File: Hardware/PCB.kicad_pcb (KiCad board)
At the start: 2 copper layers, 41 parts, among them Q5 NMOS, Q6 NMOS, Q7 NMOS, Q8 NMOS, U10 TLV379IDR, U11 LM780_TO220_MA BYC_3V_BO_POJD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, U6 ESP32-WROOM-32, U7 STM32L432KCUx, U8 IR2102, U9 IR2102

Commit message: New update
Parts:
- removed C15: C_Polarized, Capacitor_SMD:CP_Elec_5x5.3
- removed U7: STM32L432KCUx, Package_DFN_QFN:QFN-32-1EP_5x5mm_P0.5mm_EP3.45x3.45mm
- added C23: 1uF, Capacitor_SMD:C_1206_3216Metric, F.Cu at (204.2, 88.6)
- added J1: Conn_01x15, Connector_Molex:Molex_SL_171971-0015_1x15_P2.54mm_Vertical, F.Cu at (229.4, 122.9)
- added J2: Conn_01x15, Connector_Molex:Molex_SL_171971-0015_1x15_P2.54mm_Vertical, F.Cu at (238.1, 122.9)
- C13: value C -> 1uF
- D4, D6: footprint Diode_SMD:D_SOD-523 -> Diode_SMD:D_MiniMELF
- moved H3 106.7 mm to (267.4, 103.3)
- moved H4 106.7 mm to (267.4, 110.5)
- moved D4 80.1 mm to (186.8, 65.4)
- moved D6 71.1 mm to (178.3, 71.8)
- moved Q8 66.8 mm to (76.3, 90.2)
- moved Q5 66.5 mm to (41.7, 89.8)
- moved Q6 66.5 mm to (53.2, 89.8)
- moved Q7 66.5 mm to (64.8, 89.8)
- moved R9 61.3 mm to (190.6, 104.4)
- moved R11 59.7 mm to (190.0, 111.2)
- moved R13 56.2 mm to (198.1, 96.3)
- moved H1 56.1 mm to (185.9, 128.3), turned to 180 degrees
- moved R16 56.1 mm to (198.0, 108.9)
- moved R18 55.7 mm to (198.1, 104.4)
- moved R10 54.0 mm to (190.8, 99.1)
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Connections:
- C12 pad 1: /TX -> Net-(J1-Pin_4)
- D6 pad 1: Net-(D6-A) -> Net-(D6-K)
- R9 pad 1: /TX -> Net-(J1-Pin_4)
- U6 pad 1: GND -> unconnected-(U6-GND-Pad1)_23
- U6 pad 15: GND -> unconnected-(U6-GND-Pad1)_12
- U6 pad 2: Net-(U10-V+) -> unconnected-(U6-VDD-Pad2)
- U6 pad 33: unconnected-(U6-IO21-Pad33) -> /SCK
- U6 pad 36: unconnected-(U6-IO22-Pad36) -> /MISO
- U6 pad 37: unconnected-(U6-IO23-Pad37) -> /MOSI
- U6 pad 38: GND -> unconnected-(U6-GND-Pad1)_2
- U6 pad 39: GND -> unconnected-(U6-GND-Pad1)_11
- U9 pad 8: Net-(D6-A) -> Net-(D6-K)

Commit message: 1
1
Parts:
- moved H4 240.1 mm to (34.0, 54.0)
- moved H3 236.7 mm to (33.0, 70.5)
- moved H1 155.0 mm to (34.2, 96.7)
- moved H2 152.4 mm to (34.2, 106.2)
- moved U11 88.4 mm to (92.2, 127.2), turned to 0 degrees
- moved C17 75.8 mm to (109.5, 109.0)
- moved C21 71.9 mm to (112.0, 113.5), turned to 90 degrees
- moved C18 69.4 mm to (114.5, 107.5), turned to -90 degrees
- moved R15 65.4 mm to (130.5, 65.5)
- moved C1 65.3 mm to (135.5, 58.5)
- moved C16 62.0 mm to (123.0, 83.5), turned to 90 degrees
- moved R11 62.0 mm to (133.0, 87.0), turned to 180 degrees
- moved R9 61.5 mm to (141.0, 68.0), turned to -90 degrees
- moved R10 53.8 mm to (140.0, 81.5)
- moved R18 53.7 mm to (144.5, 102.1)
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
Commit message: 1
1
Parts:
- removed U6: ESP32-WROOM-32, RF_Module:ESP32-WROOM-32
- added J3: Conn_01x19, Connector_PinHeader_2.54mm:PinHeader_1x19_P2.54mm_Vertical, F.Cu at (74.2, 69.9)
- added J4: Conn_01x19, Connector_PinHeader_2.54mm:PinHeader_1x19_P2.54mm_Vertical, F.Cu at (49.2, 69.9)
- J1, J2: footprint Connector_Molex:Molex_SL_171971-0015_1x15_P2.54mm_Vertical -> Connector_PinHeader_2.54mm:PinHeader_1x15_P2.54mm_Vertical
- moved J2 163.0 mm to (115.2, 27.0), turned to 0 degrees
- moved J1 152.4 mm to (100.0, 27.0), turned to 0 degrees
- moved H4 123.1 mm to (38.0, 177.0)
- moved R14 93.2 mm to (92.5, 112.5), turned to 90 degrees
- moved C1 78.6 mm to (151.5, 135.5), turned to 90 degrees
- moved R12 77.9 mm to (141.5, 118.5), turned to -90 degrees
- moved H3 73.8 mm to (40.0, 144.0)
- moved D6 70.0 mm to (134.8, 118.5), turned to 0 degrees
- moved C12 67.0 mm to (146.5, 135.5), turned to 90 degrees
- moved R9 67.0 mm to (141.5, 135.0), turned to 90 degrees
- moved C23 63.1 mm to (127.5, 113.5), turned to 90 degrees
- moved C13 57.8 mm to (127.0, 124.5), turned to 90 degrees
- moved R15 56.6 mm to (154.0, 117.0)
- moved C19 54.7 mm to (84.3, 128.0)
- moved R19 53.5 mm to (156.5, 135.5), turned to 90 degrees
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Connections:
- J1 pad 7: unconnected-(J1-Pin_7-Pad7) -> /CC
- J2 pad 1: /RX -> /TX
- J2 pad 2: /TX -> /RX

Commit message: 1
Płytka gotowa do trasowania ścieżek
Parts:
- moved R16 59.4 mm to (98.5, 115.0)
- moved R19 52.7 mm to (140.0, 85.5), turned to -90 degrees
- moved C1 52.6 mm to (135.0, 85.5), turned to -90 degrees
- moved U10 50.3 mm to (127.0, 77.0)
- moved R17 49.9 mm to (119.0, 76.5), turned to -90 degrees
- moved R11 49.7 mm to (124.5, 85.0), turned to 180 degrees
- moved H4 47.0 mm to (40.0, 130.0)
- moved R9 44.3 mm to (127.5, 93.0), turned to 180 degrees
- moved C12 43.8 mm to (138.0, 92.5)
- moved R15 43.6 mm to (138.0, 76.5), turned to -90 degrees
- moved H2 38.7 mm to (40.0, 80.0)
- moved H3 34.0 mm to (40.0, 110.0)
- moved H1 31.7 mm to (40.0, 60.0)
- moved J3 23.2 mm to (96.0, 77.9)
- moved J4 23.2 mm to (71.0, 77.9)
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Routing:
- net Net-(Q5-D): track 0.00 -> 37.4 mm

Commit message: 1
sortowanie kluczy ok
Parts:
- moved U9 55.9 mm to (81.8, 115.1)
- moved R12 50.2 mm to (87.4, 122.1), turned to -90 degrees
- moved C23 47.4 mm to (83.3, 122.1), turned to 90 degrees
- moved C22 46.4 mm to (161.0, 136.6)
- moved D5 46.4 mm to (163.0, 90.6)
- moved L2 46.4 mm to (160.2, 101.6)
- moved R11 46.4 mm to (170.4, 91.6)
- moved U11 46.4 mm to (158.7, 127.9)
- moved C14 46.2 mm to (160.7, 113.8)
- moved C16 46.2 mm to (163.2, 122.8)
- moved C21 46.2 mm to (156.1, 122.8)
- moved R13 45.4 mm to (84.0, 109.5)
- moved D6 44.5 mm to (85.3, 126.5)
- moved U8 36.5 mm to (102.8, 115.0)
- moved R10 34.0 mm to (108.1, 121.8), turned to -90 degrees
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
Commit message: 1
ogarnieta plytka, elementy rozmieszczone, zostalo zrobic sciezki
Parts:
- moved D5 52.2 mm to (118.0, 117.1), turned to 90 degrees
- moved R11 50.3 mm to (121.0, 82.5), turned to 90 degrees
- moved L2 49.0 mm to (111.2, 102.0)
- moved C22 45.3 mm to (116.0, 131.0), turned to -90 degrees
- moved C14 37.0 mm to (126.0, 101.0)
- moved R15 33.1 mm to (115.0, 89.5)
- moved U11 32.7 mm to (127.0, 120.0)
- moved C16 32.6 mm to (132.5, 112.0)
- moved C21 32.5 mm to (125.5, 112.0), turned to 0 degrees
- moved U10 30.6 mm to (107.0, 85.9), turned to 90 degrees
- moved C12 28.8 mm to (133.0, 82.5), turned to -90 degrees
- moved R9 27.2 mm to (127.0, 82.5), turned to 90 degrees
- moved C1 26.3 mm to (121.0, 89.5), turned to 90 degrees
- moved R19 25.4 mm to (127.0, 89.5), turned to 90 degrees
- moved R17 16.4 mm to (115.0, 82.5), turned to 90 degrees
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
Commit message: 05.05.25
Mamy bledy, chujowo jest
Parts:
- moved R10 1.00 mm to (107.0, 121.8)
- moved R12 0.41 mm to (87.0, 122.1)
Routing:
- net Net-(D6-K): track 0.00 -> 14.6 mm
- net Net-(U9-HO): track 0.00 -> 12.2 mm
- net Net-(U10-V+): track 0.00 -> 5.06 mm
- net Net-(D6-A): track 0.00 -> 3.42 mm
- net Net-(Q5-D): track 37.4 -> 34.3 mm

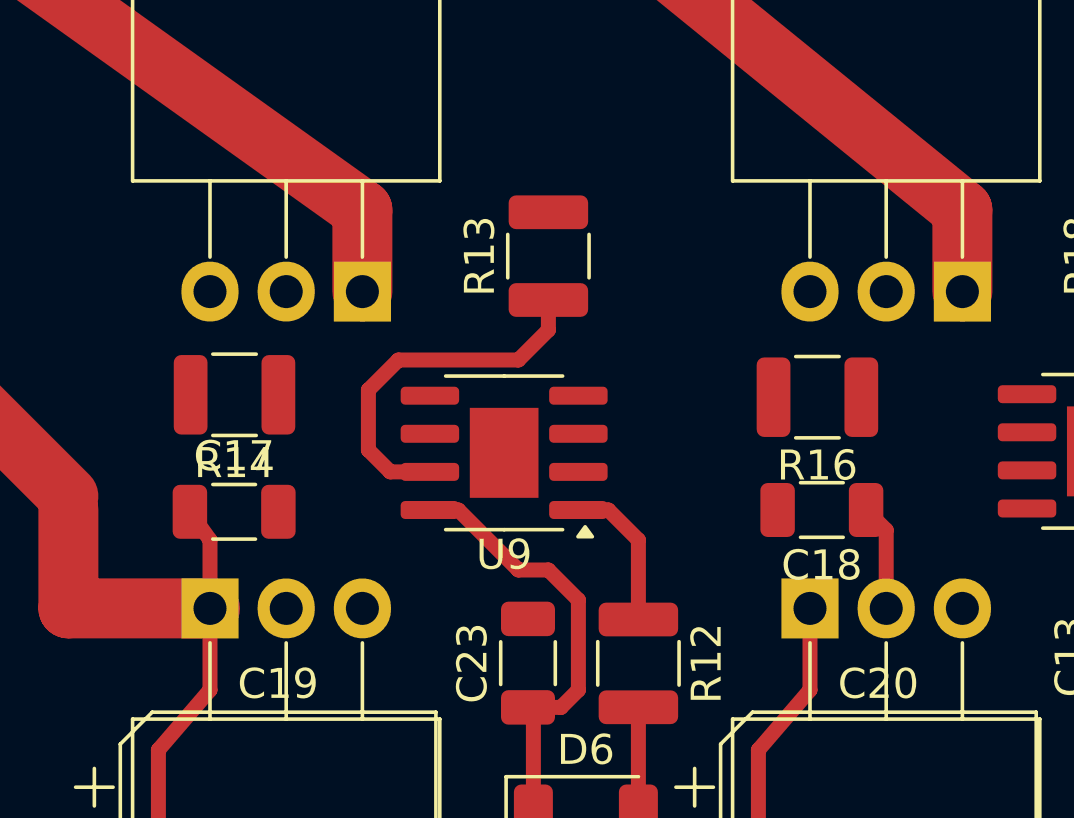
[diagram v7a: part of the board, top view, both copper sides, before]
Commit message: 09.05.25
Robimy płytkę dwustronną, jest problem z połączeniem w obrębie tranzystorów
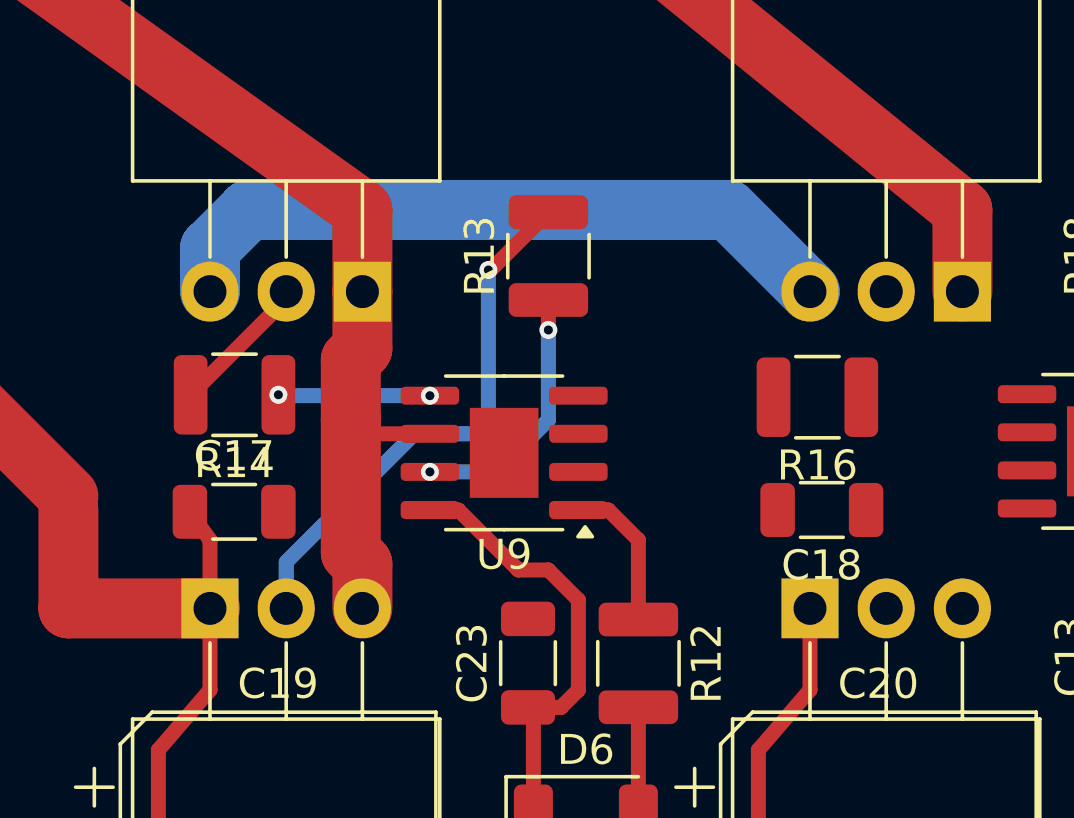
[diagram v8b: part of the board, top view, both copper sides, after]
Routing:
- net Net-(Q6-S): track 0.00 -> 23.1 mm
- net Net-(Q5-G): track 0.00 -> 18.0 mm, vias 0 -> 1
- net Net-(Q5-S): track 0.00 -> 13.7 mm
- net Net-(U9-LO): track 0.00 -> 5.06 mm, vias 0 -> 2
- net Net-(Q6-G): track 0.00 -> 4.76 mm
- net Net-(Q5-D): track 34.3 -> 30.7 mm
- net Net-(U9-HO): track 12.2 -> 8.67 mm, vias 0 -> 2
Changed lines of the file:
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@@
 	)
 	(setup
+		(stackup
+			(layer "F.SilkS"
+				(type "Top Silk Screen")
+			)
+			(layer "F.Paste"
+				(type "Top Solder Paste")
+			)
+			(layer "F.Mask"
+				(type "Top Solder Mask")
+				(thickness 0.01)
+			)
+			(layer "F.Cu"
+				(type "copper")
+				(thickness 0.035)
+			)
+			(layer "dielectric 1"
+				(type "core")
+				(thickness 1.51)
+				(material "FR4")
+				(epsilon_r 4.5)
+				(loss_tangent 0.02)
+			)
+			(layer "B.Cu"
+				(type "copper")
+				(thickness 0.035)
+			)
+			(layer "B.Mask"
+				(type "Bottom Solder Mask")
+				(thickness 0.01)
+			)
+			(layer "B.Paste"
+				(type "Bottom Solder Paste")
+			)
+			(layer "B.SilkS"
+				(type "Bottom Silk Screen")
+			)
+			(copper_finish "None")
+			(dielectric_constraints no)
+		)
 		(pad_to_mask_clearance 0)
 		(allow_soldermask_bridges_in_footprints no)
@@
 	)
 	(segment
+		(start 74 107)
+		(end 90 107)
+		(width 2)
+		(layer "B.Cu")
+		(net 1)
+	)
+	(segment
+		(start 72.72 109.72)
+		(end 72.72 108.28)
+		(width 2)
+		(layer "B.Cu")
+		(net 1)
+	)
+	(segment
+		(start 72.72 108.28)
+		(end 74 107)
+		(width 2)
+		(layer "B.Cu")
+		(net 1)
+	)
+	(segment
+		(start 90 107)
+		(end 92.72 109.72)
+		(width 2)
+		(layer "B.Cu")
+		(net 1)
+	)
+	(segment
 		(start 87 123.575)
 		(end 87 127)
@@
 	)
 	(segment
-		(start 61.46 110)
-		(end 68 116.54)
+		(start 77.4135 114)
+		(end 77.4135 112)
 		(width 2)
 		(layer "F.Cu")
-		(net 9)
+		(net 8)
 	)
 	(segment
-		(start 40 110)
-		(end 61.46 110)
+		(start 77.8 111.6135)
+		(end 77.8 109.72)
 		(width 2)
 		(layer "F.Cu")
-		(net 9)
+		(net 8)
 	)
 	(segment
-		(start 95.26 120.28)
-		(end 95.26 117.67)
+		(start 77.4135 112)
+		(end 77.8 111.6135)
+		(width 2)
+		(layer "F.Cu")
+		(net 8)
+	)
+	(segment
+		(start 77.8 118.8)
+		(end 77.4135 118.4135)
+		(width 2)
+		(layer "F.Cu")
+		(net 8)
+	)
+	(segment
+		(start 77.4135 118.4135)
+		(end 77.4135 114)
+		(width 2)
+		(layer "F.Cu")
+		(net 8)
+	)
+	(segment
+		(start 77.8735 114.46)
+		(end 77.4135 114)
 		(width 0.5)
 		(layer "F.Cu")
-		(net 9)
+		(net 8)
+	)
+	(segment
+		(start 77.8 120.28)
+		(end 77.8 118.8)
+		(width 2)
+		(layer "F.Cu")
+		(net 8)
 	)
 	(segment
-		(start 95.26 117.67)
-		(end 94.59 117)
+		(start 80.05 114.46)
+		(end 77.8735 114.46)
 		(width 0.5)
 		(layer "F.Cu")
+		(net 8)
+	)
+	(segment
+		(start 61.46 110)
+		(end 68 116.54)
+		(width 2)
+		(layer "F.Cu")
+		(net 9)
+	)
+	(segment
+		(start 40 110)
+		(end 61.46 110)
+		(width 2)
+		(layer "F.Cu")
 		(net 9)
 	)
@@
 	)
 	(segment
-		(start 78 115)
-		(end 78 113)
+		(start 82.075 109)
+		(end 82 109)
 		(width 0.5)
 		(layer "F.Cu")
-		(net 17)
+		(net 13)
 	)
 	(segment
-		(start 84 111)
-		(end 84 110)
+		(start 84 107.075)
+		(end 82.075 109)
 		(width 0.5)
 		(layer "F.Cu")
-		(net 17)
+		(net 13)
+	)
+	(via
+		(at 82 109)
+		(size 0.6)
+		(drill 0.3)
+		(layers "F.Cu" "B.Cu")
+		(net 13)
+	)
+	(segment
+		(start 82 109)
+		(end 82 114)
+		(width 0.5)
+		(layer "B.Cu")
+		(net 13)
+	)
+	(segment
+		(start 79.54 114.46)
+		(end 75.26 118.74)
+		(width 0.5)
+		(layer "B.Cu")
+		(net 13)
+	)
+	(segment
+		(start 81.54 114.46)
+		(end 79.54 114.46)
+		(width 0.5)
+		(layer "B.Cu")
+		(net 13)
+	)
+	(segment
+		(start 82 114)
+		(end 81.54 114.46)
+		(width 0.5)
+		(layer "B.Cu")
+		(net 13)
+	)
+	(segment
+		(start 75.26 118.74)
+		(end 75.26 120.28)
+		(width 0.5)
+		(layer "B.Cu")
+		(net 13)
 	)
 	(segment
-		(start 78 113)
-		(end 79 112)
+		(start 75.26 109.975)
+		(end 72.075 113.16)
 		(width 0.5)
 		(layer "F.Cu")
-		(net 17)
+		(net 14)
 	)
 	(segment
-		(start 79 112)
-		(end 83 112)
+		(start 75.26 109.72)
+		(end 75.26 109.975)
 		(width 0.5)
 		(layer "F.Cu")
+		(net 14)
+	)
+	(segment
+		(start 84 111)
+		(end 84 110)
+		(width 0.5)
+		(layer "F.Cu")
+		(net 17)
+	)
+	(via
+		(at 80.05 115.73)
+		(size 0.6)
+		(drill 0.3)
+		(layers "F.Cu" "B.Cu")
+		(net 17)
+	)
+	(via
+		(at 84 111)
+		(size 0.6)
+		(drill 0.3)
+		(layers "F.Cu" "B.Cu")
 		(net 17)
 	)
 	(segment
-		(start 83 112)
+		(start 84 114)
 		(end 84 111)
 		(width 0.5)
-		(layer "F.Cu")
+		(layer "B.Cu")
 		(net 17)
 	)
 	(segment
 		(start 80.05 115.73)
-		(end 78.73 115.73)
+		(end 82.27 115.73)
 		(width 0.5)
-		(layer "F.Cu")
+		(layer "B.Cu")
 		(net 17)
 	)
 	(segment
-		(start 78.73 115.73)
-		(end 78 115)
+		(start 82.27 115.73)
+		(end 84 114)
 		(width 0.5)
-		(layer "F.Cu")
+		(layer "B.Cu")
 		(net 17)
 	)
+	(via
+		(at 80.05 113.19)
+		(size 0.6)
+		(drill 0.3)
+		(layers "F.Cu" "B.Cu")
+		(net 18)
+	)
+	(via
+		(at 75 113.16)
+		(size 0.6)
+		(drill 0.3)
+		(layers "F.Cu" "B.Cu")
+		(net 18)
+	)
+	(segment
+		(start 75.03 113.19)
+		(end 75 113.16)
+		(width 0.5)
+		(layer "B.Cu")
+		(net 18)
+	)
+	(segment
+		(start 80.05 113.19)
+		(end 75.03 113.19)
+		(width 0.5)
+		(layer "B.Cu")
+		(net 18)
+	)
 	(segment
